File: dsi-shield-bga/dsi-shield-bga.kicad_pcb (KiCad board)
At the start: 2 copper layers, 61 parts, among them IC1 LM26480, J1 10118241-001RLF, Q1 2N7002, Q2 2N7002, Q3 Q_BSS84, Q4 2N7002, U1 XC6SLX16-FTG256, U2 MT48LC16M16A2F4, U3 MT48LC16M16A2F4

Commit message: datasheet
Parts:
- added C16: 10u, Capacitor_SMD:C_0603_1608Metric, F.Cu at (79.4, 99.0)
- added C17: 100n, Capacitor_SMD:C_0402_1005Metric, F.Cu at (82.9, 98.7)
- added IC2: M25P80-VMN6P, Package_SO:SOIC-8_7.5x5.85mm_P1.27mm, F.Cu at (106.9, 117.1)
- added P1: USB_C_Plug, Connector_USB:USB_C_Receptacle_Amphenol_12401548E4-2A, F.Cu at (82.8, 113.5)
- added U4: CH340E, Package_SO:MSOP-10-1EP_3x3mm_P0.5mm_EP1.68x1.88mm_ThermalVias, F.Cu at (43.9, 92.6)
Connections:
- U1 pad A1: Net-(U1-PadA1) -> GND
- U1 pad A16: Net-(U1-PadA16) -> GND
- U1 pad B11: Net-(U1-PadB11) -> GND
- U1 pad B4: Net-(U1-PadB4) -> Net-(U1-PadB13)
- U1 pad B7: Net-(U1-PadB7) -> GND
- U1 pad B9: Net-(U1-PadB9) -> Net-(U1-PadB13)
- U1 pad D10: Net-(U1-PadD10) -> Net-(U1-PadB13)
- U1 pad D13: Net-(U1-PadD13) -> GND
- U1 pad D4: Net-(U1-PadD4) -> GND
- U1 pad D7: Net-(U1-PadD7) -> Net-(U1-PadB13)
- U1 pad E9: Net-(U1-PadE9) -> GND
- U1 pad F11: Net-(U1-PadF11) -> Net-(U1-PadE5)
- U1 pad F8: Net-(U1-PadF8) -> Net-(U1-PadE5)
- U1 pad G10: Net-(U1-PadG10) -> Net-(U1-PadE5)
- U1 pad G13: Net-(U1-PadG13) -> Net-(U1-PadD15)
- U1 pad G15: Net-(U1-PadG15) -> GND
- U1 pad G2: Net-(U1-PadG2) -> GND
- U1 pad G4: Net-(U1-PadG4) -> Net-(U1-PadD2)
- U1 pad G8: Net-(U1-PadG8) -> GND
- U1 pad G9: Net-(U1-PadG9) -> Net-(U1-PadG7)
- U1 pad H10: Net-(U1-PadH10) -> Net-(U1-PadG7)
- U1 pad H12: Net-(U1-PadH12) -> GND
- U1 pad H6: Net-(U1-PadH6) -> Net-(U1-PadE5)
- U1 pad H7: Net-(U1-PadH7) -> GND
- U1 pad H8: Net-(U1-PadH8) -> Net-(U1-PadG7)
- U1 pad H9: Net-(U1-PadH9) -> GND
- U1 pad J10: Net-(U1-PadJ10) -> Net-(U1-PadE5)
- U1 pad J15: Net-(U1-PadJ15) -> Net-(U1-PadD15)
- U1 pad J2: Net-(U1-PadJ2) -> Net-(U1-PadD2)
- U1 pad J5: Net-(U1-PadJ5) -> GND
- U1 pad J7: Net-(U1-PadJ7) -> Net-(U1-PadG7)
- U1 pad J8: Net-(U1-PadJ8) -> GND
- U1 pad J9: Net-(U1-PadJ9) -> Net-(U1-PadG7)
- U1 pad K10: Net-(U1-PadK10) -> Net-(U1-PadG7)
- U1 pad K13: Net-(U1-PadK13) -> Net-(U1-PadD15)
- U1 pad K4: Net-(U1-PadK4) -> Net-(U1-PadD2)
- U1 pad K7: Net-(U1-PadK7) -> GND
- U1 pad K8: Net-(U1-PadK8) -> Net-(U1-PadG7)
- U1 pad K9: Net-(U1-PadK9) -> GND
- U1 pad L15: Net-(U1-PadL15) -> GND
- U1 pad L2: Net-(U1-PadL2) -> GND
- U1 pad L6: Net-(U1-PadL6) -> Net-(U1-PadE5)
- U1 pad L9: Net-(U1-PadL9) -> Net-(U1-PadE5)
- U1 pad M8: Net-(U1-PadM8) -> GND
- U1 pad N13: Net-(U1-PadN13) -> GND
- U1 pad N15: Net-(U1-PadN15) -> Net-(U1-PadD15)
- U1 pad N2: Net-(U1-PadN2) -> Net-(U1-PadD2)
- U1 pad N7: Net-(U1-PadN7) -> Net-(U1-PadN10)
- U1 pad P3: Net-(U1-PadP3) -> GND
- U1 pad R10: Net-(U1-PadR10) -> GND
- U1 pad R13: Net-(U1-PadR13) -> Net-(U1-PadD15)
- U1 pad R4: Net-(U1-PadR4) -> Net-(U1-PadN10)
- U1 pad R6: Net-(U1-PadR6) -> GND
- U1 pad R8: Net-(U1-PadR8) -> Net-(U1-PadN10)
- U1 pad T1: Net-(U1-PadT1) -> GND
- U1 pad T16: Net-(U1-PadT16) -> GND

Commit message: 20200719-1
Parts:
- added C18: 100n, Capacitor_SMD:C_0402_1005Metric, F.Cu at (130.8, 124.6)
- added C19: 100n, Capacitor_SMD:C_0402_1005Metric, F.Cu at (128.2, 129.7)
- added D5: LED, LED_SMD:LED_0603_1608Metric, F.Cu at (124.8, 130.0)
- added IC3: 25MHz, Oscillator:Oscillator_SMD_EuroQuartz_XO53-4Pin_5.0x3.2mm, F.Cu at (126.0, 126.1)
- added R26: 1k, Resistor_SMD:R_0402_1005Metric, F.Cu at (130.8, 126.6)
- added R27: 3k3, Resistor_SMD:R_0402_1005Metric, F.Cu at (133.7, 124.6)
- added R28: 3.3k, Resistor_SMD:R_0402_1005Metric, F.Cu at (128.2, 131.7)
- added R29: 1k, Resistor_SMD:R_0402_1005Metric, F.Cu at (131.1, 128.5)
- added R30: 1k, Resistor_SMD:R_0402_1005Metric, F.Cu at (133.7, 126.6)
- added R31: 0, Resistor_SMD:R_0402_1005Metric, F.Cu at (136.6, 124.6)
- added R32: 10k, Resistor_SMD:R_0402_1005Metric, F.Cu at (131.1, 130.5)
- added R33: 10k, Resistor_SMD:R_0402_1005Metric, F.Cu at (134.0, 128.5)
- added R34: 10k, Resistor_SMD:R_0402_1005Metric, F.Cu at (136.6, 126.6)
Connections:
- net Net-(U1-PadA8) renamed DBG_RX
- net Net-(U1-PadB15) renamed DSI_RESET_N
- net Net-(U1-PadB16) renamed LCD_PWREN
- net Net-(U1-PadB8) renamed DBG_TX
- net Net-(U1-PadC12) renamed TDI
- net Net-(U1-PadC14) renamed TCK
- net Net-(U1-PadC4) renamed BL_DIM
- net Net-(U1-PadC7) renamed FGPA_SCL
- net Net-(U1-PadE12) renamed DSI_GPIO1
- net Net-(U1-PadE13) renamed DSI_GPIO0
- net Net-(U1-PadE14) renamed TDO
- IC2 pad 1: Net-(IC2-Pad1) -> CFG_CS0
- IC2 pad 2: Net-(IC2-Pad2) -> CFG_MISO
- IC2 pad 4: Net-(IC2-Pad4) -> GND
- IC2 pad 5: Net-(IC2-Pad5) -> CFG_MOSI
- IC2 pad 6: Net-(IC2-Pad6) -> CFG_CLK
- IC2 pad 8: Net-(IC2-Pad8) -> +3V3
- R20 pad 2: Net-(R20-Pad2) -> DSI_CLK_P
- R21 pad 1: DSI_LP_CLK_N -> DSI_HS_CLK_N
- R21 pad 2: Net-(R21-Pad2) -> DSI_CLK_N
- R22 pad 2: Net-(R20-Pad2) -> DSI_CLK_P
- R23 pad 1: DSI_HS_CLK_N -> DSI_LP_CLK_N
- R23 pad 2: Net-(R21-Pad2) -> DSI_CLK_N
- R24 pad 1: Net-(R20-Pad2) -> DSI_CLK_P
- R24 pad 2: DSI_CLK_P -> GND
- R25 pad 1: Net-(R21-Pad2) -> DSI_CLK_N
- R25 pad 2: DSI_CLK_N -> GND
- RN1 pad 2: DSI_LP_N0 -> DSI_HS_N0
- RN1 pad 4: DSI_LP_N1 -> DSI_HS_N1
- RN1 pad 5: Net-(RN1-Pad5) -> DSI_L1_N
- RN1 pad 6: Net-(RN1-Pad6) -> DSI_L1_P
- RN1 pad 7: Net-(RN1-Pad7) -> DSI_L0_N
- RN1 pad 8: Net-(RN1-Pad8) -> DSI_L0_P
- RN2 pad 5: Net-(RN1-Pad5) -> DSI_L1_N
- RN2 pad 6: Net-(RN1-Pad6) -> DSI_L1_P
- RN2 pad 7: Net-(RN1-Pad7) -> DSI_L0_N
- RN2 pad 8: Net-(RN1-Pad8) -> DSI_L0_P
- RN3 pad 2: DSI_LP_N2 -> DSI_HS_N2
- RN3 pad 4: DSI_LP_N3 -> DSI_HS_N3
- RN3 pad 5: Net-(RN3-Pad5) -> DSI_L3_N
- RN3 pad 6: Net-(RN3-Pad6) -> DSI_L3_P
- RN3 pad 7: Net-(RN3-Pad7) -> DSI_L2_N
- RN3 pad 8: Net-(RN3-Pad8) -> DSI_L2_P
- RN4 pad 5: Net-(RN3-Pad5) -> DSI_L3_N
- RN4 pad 6: Net-(RN3-Pad6) -> DSI_L3_P
- RN4 pad 7: Net-(RN3-Pad7) -> DSI_L2_N
- RN4 pad 8: Net-(RN3-Pad8) -> DSI_L2_P
- RN5 pad 1: Net-(RN1-Pad8) -> DSI_L0_P
- RN5 pad 2: Net-(RN1-Pad7) -> DSI_L0_N
- RN5 pad 3: Net-(RN1-Pad6) -> DSI_L1_P
- RN5 pad 4: Net-(RN1-Pad5) -> DSI_L1_N
- RN5 pad 5: DSI_L1_N -> GND
- RN5 pad 6: DSI_L1_P -> GND
- RN5 pad 7: DSI_L0_N -> GND
- RN5 pad 8: DSI_L0_P -> GND
- RN6 pad 1: Net-(RN3-Pad8) -> DSI_L2_P
- RN6 pad 2: Net-(RN3-Pad7) -> DSI_L2_N
- RN6 pad 3: Net-(RN3-Pad6) -> DSI_L3_P
- RN6 pad 4: Net-(RN3-Pad5) -> DSI_L3_N
- RN6 pad 5: DSI_L3_N -> GND
- RN6 pad 6: DSI_L3_P -> GND
- RN6 pad 7: DSI_L2_N -> GND
- RN6 pad 8: DSI_L2_P -> GND
- U1 pad A15: Net-(U1-PadA15) -> TMS
- U1 pad A4: Net-(U1-PadA4) -> HPD_NOTIF
- U1 pad A5: Net-(U1-PadA5) -> TMDS0_N
- U1 pad A6: Net-(U1-PadA6) -> TMDS2_N
- U1 pad A7: Net-(U1-PadA7) -> FPGA_SDA
- U1 pad B13: Net-(U1-PadB13) -> +3V3
- U1 pad B4: Net-(U1-PadB13) -> +3V3
- U1 pad B5: Net-(U1-PadB5) -> TMDS0_P
- U1 pad B6: Net-(U1-PadB6) -> TMDS2_P
- U1 pad B9: Net-(U1-PadB13) -> +3V3
- U1 pad C15: Net-(U1-PadC15) -> DSI_HS_P1
- U1 pad C16: Net-(U1-PadC16) -> DSI_HS_N1
- U1 pad C5: Net-(U1-PadC5) -> TMDS1_N
- U1 pad D10: Net-(U1-PadB13) -> +3V3
- U1 pad D14: Net-(U1-PadD14) -> DSI_HS_P0
- U1 pad D15: Net-(U1-PadD15) -> +1V8
- U1 pad D16: Net-(U1-PadD16) -> DSI_HS_N0
- U1 pad D2: Net-(U1-PadD2) -> +1V8
- U1 pad D5: Net-(U1-PadD5) -> TMDS1_P
- U1 pad D6: Net-(U1-PadD6) -> HPD_EN
- U1 pad D7: Net-(U1-PadB13) -> +3V3
- U1 pad E15: Net-(U1-PadE15) -> DSI_LP_P2
- U1 pad E16: Net-(U1-PadE16) -> DSI_LP_N2
- U1 pad E5: Net-(U1-PadE5) -> +3V3
- U1 pad E6: Net-(U1-PadE6) -> TMDS_CLK_N
- U1 pad F11: Net-(U1-PadE5) -> +3V3
- U1 pad F12: Net-(U1-PadF12) -> DSI_LP_P0
- U1 pad F13: Net-(U1-PadF13) -> DSI_LP_P1
- U1 pad F14: Net-(U1-PadF14) -> DSI_LP_N1
- U1 pad F15: Net-(U1-PadF15) -> DSI_HS_P2
- U1 pad F16: Net-(U1-PadF16) -> DSI_HS_N2
- U1 pad F7: Net-(U1-PadF7) -> TMDS_CLK_P
- U1 pad F8: Net-(U1-PadE5) -> +3V3
- U1 pad G10: Net-(U1-PadE5) -> +3V3
- U1 pad G11: Net-(U1-PadG11) -> DSI_LP_N0
- U1 pad G12: Net-(U1-PadG12) -> DSI_LP_CLK_P
- U1 pad G13: Net-(U1-PadD15) -> +1V8
- U1 pad G14: Net-(U1-PadG14) -> DSI_LP_P3
- U1 pad G16: Net-(U1-PadG16) -> DSI_LP_N3
- U1 pad G4: Net-(U1-PadD2) -> +1V8
- U1 pad G7: Net-(U1-PadG7) -> +1V2
- U1 pad G9: Net-(U1-PadG7) -> +1V2
- U1 pad H10: Net-(U1-PadG7) -> +1V2
- U1 pad H11: Net-(U1-PadH11) -> DSI_LP_CLK_N
- U1 pad H13: Net-(U1-PadH13) -> DSI_HS_CLK_P
- U1 pad H14: Net-(U1-PadH14) -> DSI_HS_CLK_N
- U1 pad H15: Net-(U1-PadH15) -> DSI_HS_P3
- U1 pad H16: Net-(U1-PadH16) -> DSI_HS_N3
- U1 pad H6: Net-(U1-PadE5) -> +3V3
- U1 pad H8: Net-(U1-PadG7) -> +1V2
- U1 pad J10: Net-(U1-PadE5) -> +3V3
- U1 pad J15: Net-(U1-PadD15) -> +1V8
- U1 pad J2: Net-(U1-PadD2) -> +1V8
- U1 pad J7: Net-(U1-PadG7) -> +1V2
- U1 pad J9: Net-(U1-PadG7) -> +1V2
- U1 pad K10: Net-(U1-PadG7) -> +1V2
- U1 pad K13: Net-(U1-PadD15) -> +1V8
- U1 pad K4: Net-(U1-PadD2) -> +1V8
- U1 pad K8: Net-(U1-PadG7) -> +1V2
- U1 pad L6: Net-(U1-PadE5) -> +3V3
- U1 pad L9: Net-(U1-PadE5) -> +3V3
- U1 pad N15: Net-(U1-PadD15) -> +1V8
- U1 pad N2: Net-(U1-PadD2) -> +1V8
- U1 pad P10: Net-(U1-PadP10) -> CFG_MISO
- U1 pad P14: Net-(U1-PadP14) -> GND
- U1 pad R11: Net-(U1-PadR11) -> CFG_CLK
- U1 pad R13: Net-(U1-PadD15) -> +1V8
- U1 pad T10: Net-(U1-PadT10) -> CFG_MOSI
- U1 pad T11: Net-(U1-PadT11) -> CFG_M0
- U1 pad T3: Net-(U1-PadT3) -> CFG_CS0

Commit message: pcb
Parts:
- moved C13 111.1 mm to (53.6, 98.7)
- moved R12 111.1 mm to (53.6, 100.7)
- moved R17 111.1 mm to (56.5, 100.7)
- moved R19 111.1 mm to (59.4, 98.2)
- moved C6 110.3 mm to (57.0, 74.4), turned to 180 degrees
- moved C7 105.0 mm to (58.2, 80.5)
- moved C8 103.5 mm to (57.7, 88.5)
- moved R11 102.0 mm to (67.8, 91.4), turned to 90 degrees
- moved L2 101.7 mm to (61.8, 69.8)
- moved C3 101.0 mm to (57.6, 90.7)
- moved C11 100.8 mm to (62.9, 75.6)
- moved R14 98.2 mm to (72.3, 87.8), turned to 180 degrees
- moved C5 98.0 mm to (63.0, 85.3)
- moved C10 95.0 mm to (72.0, 90.1)
- moved R16 87.6 mm to (85.6, 91.2)
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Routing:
- net SDRAM_RAS_N: track 0.71 -> 0.00 mm, vias 1 -> 0
- net SDRAM_DQM1: track 0.71 -> 0.00 mm, vias 1 -> 0
- net SDRAM_DQM0: track 0.71 -> 0.00 mm, vias 1 -> 0
- net SDRAM_DQ8: track 0.71 -> 0.00 mm, vias 1 -> 0
- net SDRAM_DQ6: track 0.71 -> 0.00 mm, vias 1 -> 0
- net SDRAM_DQ4: track 0.71 -> 0.00 mm, vias 1 -> 0
- net SDRAM_DQ2: track 0.71 -> 0.00 mm, vias 1 -> 0
- net SDRAM_DQ14: track 0.71 -> 0.00 mm, vias 1 -> 0
- net SDRAM_DQ12: track 0.71 -> 0.00 mm, vias 1 -> 0
- net SDRAM_DQ10: track 0.71 -> 0.00 mm, vias 1 -> 0
- net SDRAM_DQ0: track 0.71 -> 0.00 mm, vias 1 -> 0
- net SDRAM_CKE: track 0.71 -> 0.00 mm, vias 1 -> 0
- net SDRAM_CAS_N: track 0.71 -> 0.00 mm, vias 1 -> 0
- net SDRAM_A8: track 0.71 -> 0.00 mm, vias 1 -> 0
- net SDRAM_A7: track 0.71 -> 0.00 mm, vias 1 -> 0
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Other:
- board outline added: 100 x 100 mm

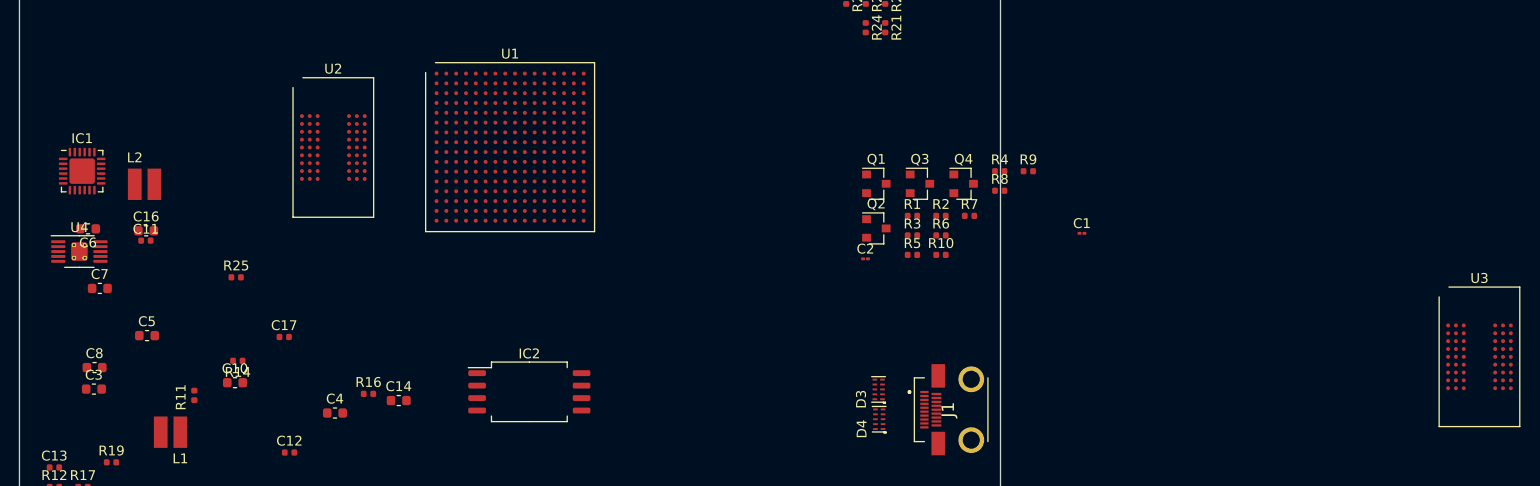
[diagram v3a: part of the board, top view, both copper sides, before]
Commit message: ddr sdram
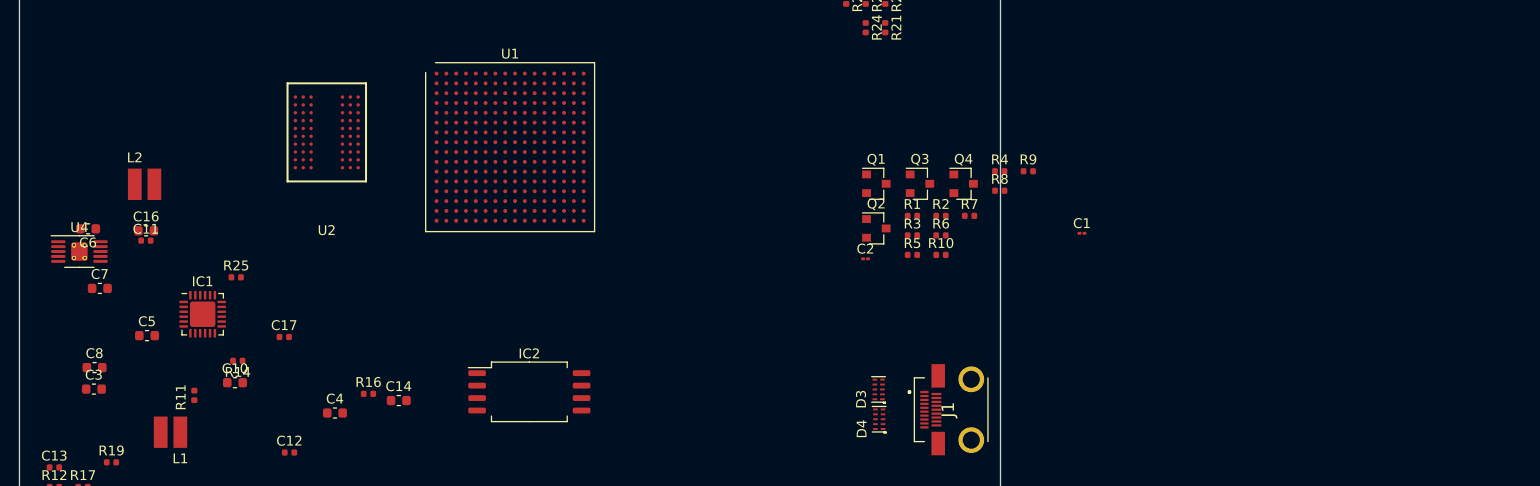
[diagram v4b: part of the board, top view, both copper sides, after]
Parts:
- removed U3: MT48LC16M16A2F4, Gekkio_Package_BGA:Micron_VFBGA-54_8x14mm_Layout9x9_P0.8mm
- U2: value MT48LC16M16A2F4 -> K4X1G163PE; footprint Gekkio_Package_BGA:Micron_VFBGA-54_8x14mm_Layout9x9_P0.8mm -> mybays:FBGA60-6X10
- moved IC1 19.1 mm to (68.7, 83.1)
- moved U2 1.68 mm to (81.3, 64.5)
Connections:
- net Net-(U2-PadE2) renamed SDRAM_DQS1
- U2 pad B1: SDRAM_DQ14 -> Net-(U2-PadB1)
- U2 pad B3: Net-(U2-PadB3) -> SDRAM_DQ14
- U2 pad B7: Net-(U2-PadB7) -> SDRAM_DQ1
- U2 pad B9: SDRAM_DQ1 -> Net-(U2-PadB9)
- U2 pad C1: SDRAM_DQ12 -> Net-(U2-PadC1)
- U2 pad C3: Net-(U2-PadC3) -> SDRAM_DQ12
- U2 pad C7: Net-(U2-PadC7) -> SDRAM_DQ3
- U2 pad C9: SDRAM_DQ3 -> Net-(U2-PadC9)
- U2 pad D1: SDRAM_DQ10 -> Net-(U2-PadD1)
- U2 pad D3: Net-(U2-PadD3) -> SDRAM_DQ10
- U2 pad D7: Net-(U2-PadD7) -> SDRAM_DQ5
- U2 pad D9: SDRAM_DQ5 -> Net-(U2-PadD9)
- U2 pad E1: SDRAM_DQ8 -> Net-(U2-PadE1)
- U2 pad E3: Net-(U2-PadE3) -> SDRAM_DQ8
- U2 pad E7: Net-(U2-PadE7) -> SDRAM_DQ7
- U2 pad E8: SDRAM_DQM0 -> SDRAM_DQS0
- U2 pad E9: SDRAM_DQ7 -> Net-(U2-PadE9)
- U2 pad F1: SDRAM_DQM1 -> Net-(U2-PadF1)
- U2 pad F2: SDRAM_CLK -> SDRAM_DQM1
- U2 pad F3: SDRAM_CKE -> Net-(U2-PadF3)
- U2 pad F7: SDRAM_CAS_N -> /Sheet5F261984/SDRAM_A13
- U2 pad F8: SDRAM_RAS_N -> SDRAM_DQM0
- U2 pad F9: SDRAM_WE_N -> Net-(U2-PadF9)
- U2 pad G1: SDRAM_A12 -> SDRAM_CKE
- U2 pad G2: SDRAM_A11 -> SDRAM_CLK
- U2 pad G3: SDRAM_A9 -> SDRAM_CLK_N
- U2 pad G7: SDRAM_BA0 -> SDRAM_WE_N
- U2 pad G8: SDRAM_BA1 -> SDRAM_CAS_N
- U2 pad G9: SDRAM_CS_N -> SDRAM_RAS_N
- U2 pad H1: SDRAM_A8 -> SDRAM_A9
- U2 pad H2: SDRAM_A7 -> SDRAM_A11
- U2 pad H3: SDRAM_A6 -> SDRAM_A12
- U2 pad H7: SDRAM_A0 -> SDRAM_CS_N
- U2 pad H8: SDRAM_A1 -> SDRAM_BA0
- U2 pad H9: SDRAM_A10 -> SDRAM_BA1
- U2 pad J1: Net-(U2-PadJ1) -> SDRAM_A6
- U2 pad J2: SDRAM_A5 -> SDRAM_A7
- U2 pad J3: SDRAM_A4 -> SDRAM_A8
- U2 pad J7: SDRAM_A3 -> SDRAM_A10
- U2 pad J8: SDRAM_A2 -> SDRAM_A0
- U2 pad J9: Net-(U2-PadJ9) -> SDRAM_A1

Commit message: 20200808
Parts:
- removed RN1, RN3: 160, Resistor_SMD:R_Array_Convex_4x0402
- removed RN2, RN4: 22, Resistor_SMD:R_Array_Convex_4x0402
- removed RN5, RN6: 51, Resistor_SMD:R_Array_Convex_4x0402
- added C20: 1u, Capacitor_SMD:C_0402_1005Metric, F.Cu at (162.0, 95.0)
- added C21: 100n, Capacitor_SMD:C_0402_1005Metric, F.Cu at (162.0, 97.0)
- added C22: 100n, Capacitor_SMD:C_0402_1005Metric, F.Cu at (164.9, 95.0)
- added C23: 100n, Capacitor_SMD:C_0402_1005Metric, F.Cu at (162.0, 99.0)
- added C24: 100n, Capacitor_SMD:C_0402_1005Metric, F.Cu at (164.9, 97.0)
- added C25: 100n, Capacitor_SMD:C_0402_1005Metric, F.Cu at (167.8, 95.0)
- added C26: 100n, Capacitor_SMD:C_0402_1005Metric, F.Cu at (164.9, 99.0)
- added C27: 10n, Capacitor_SMD:C_0402_1005Metric, F.Cu at (167.8, 97.0)
- added C28: 10n, Capacitor_SMD:C_0402_1005Metric, F.Cu at (170.7, 95.0)
- added C29: 10n, Capacitor_SMD:C_0402_1005Metric, F.Cu at (167.8, 99.0)
- added C30: 1u, Capacitor_SMD:C_0402_1005Metric, F.Cu at (166.0, 114.0)
- added C31: 100n, Capacitor_SMD:C_0402_1005Metric, F.Cu at (166.0, 116.0)
- added C32: 100n, Capacitor_SMD:C_0402_1005Metric, F.Cu at (168.9, 114.0)
- added C33: 100n, Capacitor_SMD:C_0402_1005Metric, F.Cu at (166.0, 118.0)
- added C34: 100n, Capacitor_SMD:C_0402_1005Metric, F.Cu at (168.9, 116.0)
- added C35: 100n, Capacitor_SMD:C_0402_1005Metric, F.Cu at (171.8, 114.0)
- added C36: 100n, Capacitor_SMD:C_0402_1005Metric, F.Cu at (166.0, 120.0)
- added C37: 10n, Capacitor_SMD:C_0402_1005Metric, F.Cu at (168.9, 118.0)
- added C38: 10n, Capacitor_SMD:C_0402_1005Metric, F.Cu at (171.8, 116.0)
- added C39: 10n, Capacitor_SMD:C_0402_1005Metric, F.Cu at (174.7, 114.0)
- added C40: 100n, Capacitor_SMD:C_0402_1005Metric, F.Cu at (168.9, 120.0)
- added C41: 100n, Capacitor_SMD:C_0402_1005Metric, F.Cu at (171.8, 118.0)
- added C42: 4.7u, Capacitor_SMD:C_0805_2012Metric, F.Cu at (178.0, 83.0)
- added C43: 1u, Capacitor_SMD:C_0603_1608Metric_Pad1.05x0.95mm_HandSolder, F.Cu at (182.4, 82.8)
- added C44: 1u, Capacitor_SMD:C_0603_1608Metric_Pad1.05x0.95mm_HandSolder, F.Cu at (188.5, 80.4)
- added C45: 22p, Capacitor_SMD:C_0402_1005Metric, F.Cu at (186.0, 82.7)
- added C46: 4.7u, Capacitor_SMD:C_0805_2012Metric, F.Cu at (184.2, 79.7)
- added C47: 4.7u, Capacitor_SMD:C_0805_2012Metric, F.Cu at (199.0, 173.0)
- added C48: 1u, Capacitor_SMD:C_0603_1608Metric_Pad1.05x0.95mm_HandSolder, F.Cu at (203.4, 172.8)
- added C49: 22p, Capacitor_SMD:C_0402_1005Metric, F.Cu at (201.8, 175.5)
- added CN1: Header_6, dsi_shield:Header 6x1 8.5mm, F.Cu at (163.0, 69.0)
- added D6: Diode_Schottky, dsi_shield:SOD3715X145N, F.Cu at (178.9, 76.6)
- added D7: Diode_Schottky, dsi_shield:SOD3715X145N, F.Cu at (178.9, 79.9)
- added D8: Diode_Schottky, dsi_shield:SOD3715X145N, F.Cu at (185.0, 76.6)
- added D9: Diode_Schottky, dsi_shield:SOD3715X145N, F.Cu at (193.7, 173.2)
- added IC10: MT46V32M16P-5B:F, dsi_shield:TSOP66, B.Cu at (65.9, 92.1)
- added IC4: SOT95P275X110-5N, mybays:SOT95P275X110-5N, F.Cu at (183.0, 59.0)
- added IC5: SOT95P275X110-5N, mybays:SOT95P275X110-5N, F.Cu at (193.3, 177.1)
- added J2: Conn_02x15_Odd_Even, Connector_PinHeader_2.54mm:PinHeader_2x15_P2.54mm_Vertical, F.Cu at (141.0, 101.0)
- added L3: 4.7uH, dsi_shield:IND_PANASONIC_ELLVEG, F.Cu at (189.3, 77.1)
- added L4: 4.7uH, dsi_shield:IND_PANASONIC_ELLVEG, F.Cu at (197.1, 176.9)
- added R35: 0, Resistor_SMD:R_0402_1005Metric, F.Cu at (140.0, 146.0)
- added R36: 1k, Resistor_SMD:R_0402_1005Metric, F.Cu at (89.5, 41.0)
- added R37: 0, Resistor_SMD:R_0402_1005Metric, F.Cu at (142.9, 146.0)
- added R38: 1k, Resistor_SMD:R_0402_1005Metric, F.Cu at (177.6, 114.0)
- added R39: 1k, Resistor_SMD:R_0402_1005Metric, F.Cu at (171.8, 120.0)
- added R40: 100, Resistor_SMD:R_0402_1005Metric, F.Cu at (132.0, 138.0)
- added R41: 100k, Resistor_SMD:R_0402_1005Metric, F.Cu at (192.2, 80.2)
- added R42: 100k, Resistor_SMD:R_0402_1005Metric, F.Cu at (188.9, 82.7)
- added R43: 27k, Resistor_SMD:R_0402_1005Metric, F.Cu at (192.2, 82.2)
- added R44: 100k, Resistor_SMD:R_0402_1005Metric, F.Cu at (201.8, 177.5)
- added R45: 27k, Resistor_SMD:R_0402_1005Metric, F.Cu at (204.7, 175.0)
- added R46: 160, Resistor_SMD:R_0402_1005Metric, F.Cu at (127.4, 75.8)
- added R47: 160, Resistor_SMD:R_0402_1005Metric, F.Cu at (127.4, 76.8)
- added R48: 22, Resistor_SMD:R_0402_1005Metric, F.Cu at (127.4, 74.8)
- added R49: 22, Resistor_SMD:R_0402_1005Metric, F.Cu at (127.4, 77.8)
- added R50: 51, Resistor_SMD:R_0402_1005Metric, B.Cu at (130.8, 75.8)
- added R51: 51, Resistor_SMD:R_0402_1005Metric, B.Cu at (130.8, 76.8)
- added R52: 160, Resistor_SMD:R_0402_1005Metric, F.Cu at (127.4, 79.8)
- added R53: 160, Resistor_SMD:R_0402_1005Metric, F.Cu at (127.4, 80.8)
- added R54: 22, Resistor_SMD:R_0402_1005Metric, F.Cu at (127.4, 78.8)
- added R55: 22, Resistor_SMD:R_0402_1005Metric, F.Cu at (127.4, 81.9)
- added R56: 51, Resistor_SMD:R_0402_1005Metric, B.Cu at (130.8, 79.8)
- added R57: 51, Resistor_SMD:R_0402_1005Metric, B.Cu at (130.8, 80.8)
- added R58: 160, Resistor_SMD:R_0402_1005Metric, F.Cu at (127.4, 87.9)
- added R59: 160, Resistor_SMD:R_0402_1005Metric, F.Cu at (127.4, 88.9)
- added R60: 22, Resistor_SMD:R_0402_1005Metric, F.Cu at (127.4, 86.9)
- added R61: 22, Resistor_SMD:R_0402_1005Metric, F.Cu at (127.4, 89.9)
- added R62: 51, Resistor_SMD:R_0402_1005Metric, B.Cu at (130.8, 87.9)
- added R63: 51, Resistor_SMD:R_0402_1005Metric, B.Cu at (130.8, 88.9)
- added R64: 160, Resistor_SMD:R_0402_1005Metric, F.Cu at (127.4, 92.1)
- added R65: 160, Resistor_SMD:R_0402_1005Metric, F.Cu at (127.4, 93.1)
- added R66: 22, Resistor_SMD:R_0402_1005Metric, F.Cu at (127.4, 91.0)
- added R67: 22, Resistor_SMD:R_0402_1005Metric, F.Cu at (127.4, 94.1)
- added R68: 51, Resistor_SMD:R_0402_1005Metric, B.Cu at (130.8, 92.0)
- added R69: 51, Resistor_SMD:R_0402_1005Metric, B.Cu at (130.8, 93.1)
- IC2: footprint Package_SO:SOIC-8_7.5x5.85mm_P1.27mm -> Package_DFN_QFN:DFN-8-1EP_6x5mm_P1.27mm_EP4x4mm
- IC3: footprint Oscillator:Oscillator_SMD_EuroQuartz_XO53-4Pin_5.0x3.2mm -> Oscillator:Oscillator_SMD_Abracon_ASE-4Pin_3.2x2.5mm_HandSoldering
- R24, R25: moved to B.Cu
- R31: value 0 -> 1k
- moved R19 95.6 mm to (114.9, 176.0)
- moved C13 95.6 mm to (109.1, 176.5)
- moved C18 93.8 mm to (190.0, 144.1)
- moved R27 93.8 mm to (192.9, 144.1)
- moved R31 93.8 mm to (195.8, 144.1)
- moved R32 93.8 mm to (190.3, 150.0)
- moved C19 93.8 mm to (187.4, 149.2)
- moved D5 93.8 mm to (183.9, 149.5)
- moved IC3 93.8 mm to (185.2, 145.6)
- moved R26 93.8 mm to (190.0, 146.0)
- moved R28 93.8 mm to (187.4, 151.2)
- moved R29 93.8 mm to (190.3, 148.0)
- moved R30 93.8 mm to (192.9, 146.0)
- moved R33 93.8 mm to (193.2, 148.0)
- moved R34 93.8 mm to (195.8, 146.0)
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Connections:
- net BL_DIM renamed /Sheet5F173767/BL_DIM
- net CFG_CLK renamed /Sheet5F173767/QSPI_CLK
- net CFG_CS0 renamed /Sheet5F173767/QSPI_CS0
- net CFG_M0 renamed /Sheet5F173767/FPGA_M0
- net CFG_MISO renamed /Sheet5F173767/QSPI_DQ1
- net CFG_MOSI renamed /Sheet5F173767/QSPI_DQ0
- net CLK_25MHZ renamed /Sheet5F173767/CLK_25MHZ
- net FPGA_SDA renamed /Sheet5F173767/SDA
- net HPD_EN renamed /Sheet5F173767/HPD_EN
- net HPD_NOTIF renamed /Sheet5F173767/HPD_NOTIFY
- net SDRAM_A0 renamed /Sheet5F173767/SDRAM_A0
- net SDRAM_A1 renamed /Sheet5F173767/SDRAM_A1
- net SDRAM_A10 renamed /Sheet5F173767/SDRAM_A10
- net SDRAM_A11 renamed /Sheet5F173767/SDRAM_A11
- net SDRAM_A12 renamed /Sheet5F173767/SDRAM_A12
- net SDRAM_A2 renamed /Sheet5F173767/SDRAM_A2
- net SDRAM_A3 renamed /Sheet5F173767/SDRAM_A3
- net SDRAM_A4 renamed /Sheet5F173767/SDRAM_A4
- net SDRAM_A5 renamed /Sheet5F173767/SDRAM_A5
- net SDRAM_A6 renamed /Sheet5F173767/SDRAM_A6
- net SDRAM_A7 renamed /Sheet5F173767/SDRAM_A7
- net SDRAM_A8 renamed /Sheet5F173767/SDRAM_A8
- net SDRAM_A9 renamed /Sheet5F173767/SDRAM_A9
- net SDRAM_CAS_N renamed /Sheet5F173767/SDRAM_CAS_N
- net SDRAM_CKE renamed /Sheet5F173767/SDRAM_CKE
- net SDRAM_DQ0 renamed /Sheet5F173767/SDRAM_DQ0
- net SDRAM_DQ1 renamed /Sheet5F173767/SDRAM_DQ1
- net SDRAM_DQ10 renamed /Sheet5F173767/SDRAM_DQ10
- net SDRAM_DQ11 renamed /Sheet5F173767/SDRAM_DQ11
- net SDRAM_DQ12 renamed /Sheet5F173767/SDRAM_DQ12
- net SDRAM_DQ13 renamed /Sheet5F173767/SDRAM_DQ13
- net SDRAM_DQ14 renamed /Sheet5F173767/SDRAM_DQ14
- net SDRAM_DQ15 renamed /Sheet5F173767/SDRAM_DQ15
- net SDRAM_DQ2 renamed /Sheet5F173767/SDRAM_DQ2
- net SDRAM_DQ3 renamed /Sheet5F173767/SDRAM_DQ3
- net SDRAM_DQ4 renamed /Sheet5F173767/SDRAM_DQ4
- net SDRAM_DQ5 renamed /Sheet5F173767/SDRAM_DQ5
- net SDRAM_DQ6 renamed /Sheet5F173767/SDRAM_DQ6
- net SDRAM_DQ7 renamed /Sheet5F173767/SDRAM_DQ7
- net SDRAM_DQ8 renamed /Sheet5F173767/SDRAM_DQ8
- net SDRAM_DQ9 renamed /Sheet5F173767/SDRAM_DQ9
- net SDRAM_DQM0 renamed /Sheet5F173767/SDRAM_DQM0
- net SDRAM_DQM1 renamed /Sheet5F173767/SDRAM_DQM1
- net SDRAM_RAS_N renamed /Sheet5F173767/SDRAM_RAS_N
- net SDRAM_WE_N renamed /Sheet5F173767/SDRAM_WE_N
- net TMDS0_N renamed /Sheet5F173767/TMDS0_N
- net TMDS0_P renamed /Sheet5F173767/TMDS0_P
- net TMDS1_N renamed /Sheet5F173767/TMDS1_N
- net TMDS1_P renamed /Sheet5F173767/TMDS1_P
- net TMDS2_N renamed /Sheet5F173767/TMDS2_N
- net TMDS2_P renamed /Sheet5F173767/TMDS2_P
- net TMDS_CLK_N renamed /Sheet5F173767/TMDS_CLK_N
- net TMDS_CLK_P renamed /Sheet5F173767/TMDS_CLK_P
- net TMS renamed FPGA_TMS
- IC2 pad 3: Net-(IC2-Pad3) -> /Sheet5F173767/QSPI_DQ2
- IC2 pad 7: Net-(IC2-Pad7) -> /Sheet5F173767/QSPI_DQ3
- P1 pad A1: Net-(P1-PadA1) -> GND
- P1 pad A12: Net-(P1-PadA1) -> GND
- P1 pad B1: Net-(P1-PadA1) -> GND
- P1 pad B12: Net-(P1-PadA1) -> GND
- P1 pad S1: Net-(P1-PadS1) -> GND
- Q2 pad 3: FPGA_SCL -> /Sheet5F173767/SCL
- R26 pad 2: +2V5 -> +3V3
- R27 pad 2: +2V5 -> +3V3
- R31 pad 2: +2V5 -> +3V3
- R32 pad 2: Net-(IC2-Pad3) -> /Sheet5F173767/QSPI_DQ2
- R33 pad 2: Net-(IC2-Pad7) -> /Sheet5F173767/QSPI_DQ3
- R7 pad 2: FPGA_SCL -> /Sheet5F173767/SCL
- U1 pad A3: Net-(U1-PadA3) -> /Sheet5F173767/DDR_VREF
- U1 pad A8: DBG_RX -> /Sheet5F173767/DBG_RX
- U1 pad B8: DBG_TX -> /Sheet5F12EB4F/DBG_RX
- U1 pad C12: TDI -> FPGA_TDI
- U1 pad C14: TCK -> FPGA_TCK
- U1 pad C15: DSI_HS_P1 -> Net-(U1-PadC15)
- U1 pad C16: DSI_HS_N1 -> Net-(U1-PadC16)
- U1 pad C2: Net-(U1-PadC2) -> /Sheet5F173767/SDRAM_BA1
- U1 pad C3: Net-(U1-PadC3) -> /Sheet5F173767/SDRAM_BA0
- U1 pad C7: FGPA_SCL -> /Sheet5F173767/SCL
- U1 pad D14: DSI_HS_P0 -> Net-(U1-PadD14)
- U1 pad D16: DSI_HS_N0 -> Net-(U1-PadD16)
- U1 pad D2: +1V8 -> V_DDR
- U1 pad E1: Net-(U1-PadE1) -> /Sheet5F173767/SDRAM_CLK_N
- U1 pad E14: TDO -> FPGA_TDO
- U1 pad E15: DSI_LP_P2 -> Net-(U1-PadE15)
- U1 pad E16: DSI_LP_N2 -> Net-(U1-PadE16)
- U1 pad E2: Net-(U1-PadE2) -> /Sheet5F173767/SDRAM_CLK_P
- U1 pad F12: DSI_LP_P0 -> Net-(U1-PadF12)
- U1 pad F13: DSI_LP_P1 -> Net-(U1-PadF13)
- U1 pad F14: DSI_LP_N1 -> Net-(U1-PadF14)
- U1 pad F15: DSI_HS_P2 -> Net-(U1-PadF15)
- U1 pad F16: DSI_HS_N2 -> Net-(U1-PadF16)
- U1 pad G11: DSI_LP_N0 -> Net-(U1-PadG11)
- U1 pad G12: DSI_LP_CLK_P -> Net-(U1-PadG12)
- U1 pad G14: DSI_LP_P3 -> Net-(U1-PadG14)
- U1 pad G16: DSI_LP_N3 -> Net-(U1-PadG16)
- U1 pad G4: +1V8 -> V_DDR
- U1 pad H11: DSI_LP_CLK_N -> Net-(U1-PadH11)
- U1 pad H13: DSI_HS_CLK_P -> Net-(U1-PadH13)
- U1 pad H14: DSI_HS_CLK_N -> Net-(U1-PadH14)
- U1 pad H15: DSI_HS_P3 -> DSI_HS_CLK_P
- U1 pad H16: DSI_HS_N3 -> DSI_HS_CLK_N
- U1 pad H2: Net-(U1-PadH2) -> /Sheet5F173767/SDRAM_DQS0
- U1 pad J14: Net-(U1-PadJ14) -> DSI_LP_CLK_P
- U1 pad J16: Net-(U1-PadJ16) -> DSI_LP_CLK_N
- U1 pad J2: +1V8 -> V_DDR
- U1 pad K4: +1V8 -> V_DDR
- U1 pad L5: Net-(U1-PadL5) -> /Sheet5F173767/SDRAM_CS_N
- U1 pad M3: Net-(U1-PadM3) -> /Sheet5F173767/DDR_VREF
- U1 pad N10: Net-(U1-PadN10) -> +3V3
- U1 pad N12: Net-(U1-PadN12) -> /Sheet5F173767/QSPI_DQ2
- U1 pad N2: +1V8 -> V_DDR
- U1 pad N3: Net-(U1-PadN3) -> /Sheet5F173767/SDRAM_DQS1
- U1 pad N7: Net-(U1-PadN10) -> +3V3
- U1 pad P12: Net-(U1-PadP12) -> /Sheet5F173767/QSPI_DQ3
- U1 pad R4: Net-(U1-PadN10) -> +3V3
- U1 pad R8: Net-(U1-PadN10) -> +3V3
- U2 pad A1: Net-(U2-PadA1) -> GND
- U2 pad A3: Net-(U2-PadA3) -> GND
- U2 pad A7: Net-(U2-PadA7) -> V_DDR
- U2 pad A9: Net-(U2-PadA9) -> V_DDR
- U2 pad B1: Net-(U2-PadB1) -> V_DDR
- U2 pad B9: Net-(U2-PadB9) -> GND
- U2 pad C1: Net-(U2-PadC1) -> GND
- U2 pad C9: Net-(U2-PadC9) -> V_DDR
- U2 pad D1: Net-(U2-PadD1) -> V_DDR
- U2 pad D9: Net-(U2-PadD9) -> GND
- U2 pad E1: Net-(U2-PadE1) -> GND
- U2 pad E2: SDRAM_DQS1 -> /Sheet5F173767/SDRAM_DQS1
- U2 pad E8: SDRAM_DQS0 -> /Sheet5F173767/SDRAM_DQS0
- U2 pad E9: Net-(U2-PadE9) -> V_DDR
- U2 pad F1: Net-(U2-PadF1) -> GND
- U2 pad F7: /Sheet5F261984/SDRAM_A13 -> /Sheet5F173767/SDRAM_A13
- U2 pad F9: Net-(U2-PadF9) -> V_DDR
- U2 pad G2: SDRAM_CLK -> /Sheet5F173767/SDRAM_CLK_P
- U2 pad G3: SDRAM_CLK_N -> /Sheet5F173767/SDRAM_CLK_N
- U2 pad H7: SDRAM_CS_N -> /Sheet5F173767/SDRAM_CS_N
- U2 pad H8: SDRAM_BA0 -> /Sheet5F173767/SDRAM_BA0
- U2 pad H9: SDRAM_BA1 -> /Sheet5F173767/SDRAM_BA1
- U2 pad K1: Net-(U2-PadK1) -> GND
- U2 pad K9: Net-(U2-PadK9) -> V_DDR
- U4 pad 4: Net-(U4-Pad4) -> CPU_RST
- U4 pad 8: TXD -> /Sheet5F173767/DBG_RX
- U4 pad 9: RXD -> /Sheet5F12EB4F/DBG_RX
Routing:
- net GND: track 0.00 -> 48.8 mm, vias 0 -> 69
- net +3V3: track 0.00 -> 36.1 mm, vias 0 -> 51
- net +1V2: track 0.00 -> 17.0 mm, vias 0 -> 24
- net +1V8: track 0.00 -> 12.7 mm, vias 0 -> 18
- net V_DDR: track 0.00 -> 10.6 mm, vias 0 -> 15
- net Net-(R36-Pad1): track 0.00 -> 2.12 mm, vias 0 -> 3
- net Net-(R27-Pad1): track 0.00 -> 2.12 mm, vias 0 -> 3
- net Net-(D5-Pad2): track 0.00 -> 2.12 mm, vias 0 -> 3
- net FPGA_TDO: track 0.00 -> 2.12 mm, vias 0 -> 3
- net FPGA_TDI: track 0.00 -> 2.12 mm, vias 0 -> 3
- net FPGA_TCK: track 0.00 -> 2.12 mm, vias 0 -> 3
- net DSI_RESET_N: track 0.00 -> 2.12 mm, vias 0 -> 3
- net DSI_LP_CLK_P: track 0.00 -> 2.12 mm, vias 0 -> 3
- net DSI_HS_CLK_P: track 0.00 -> 2.12 mm, vias 0 -> 3
- net DSI_GPIO1: track 0.00 -> 2.12 mm, vias 0 -> 3
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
